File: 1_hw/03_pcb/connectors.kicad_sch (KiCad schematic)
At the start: 15 parts, among them J1 TYPE-C-31-M-12, J2 SMA, J3 SMA, J4 BNC, J5 PH-00244

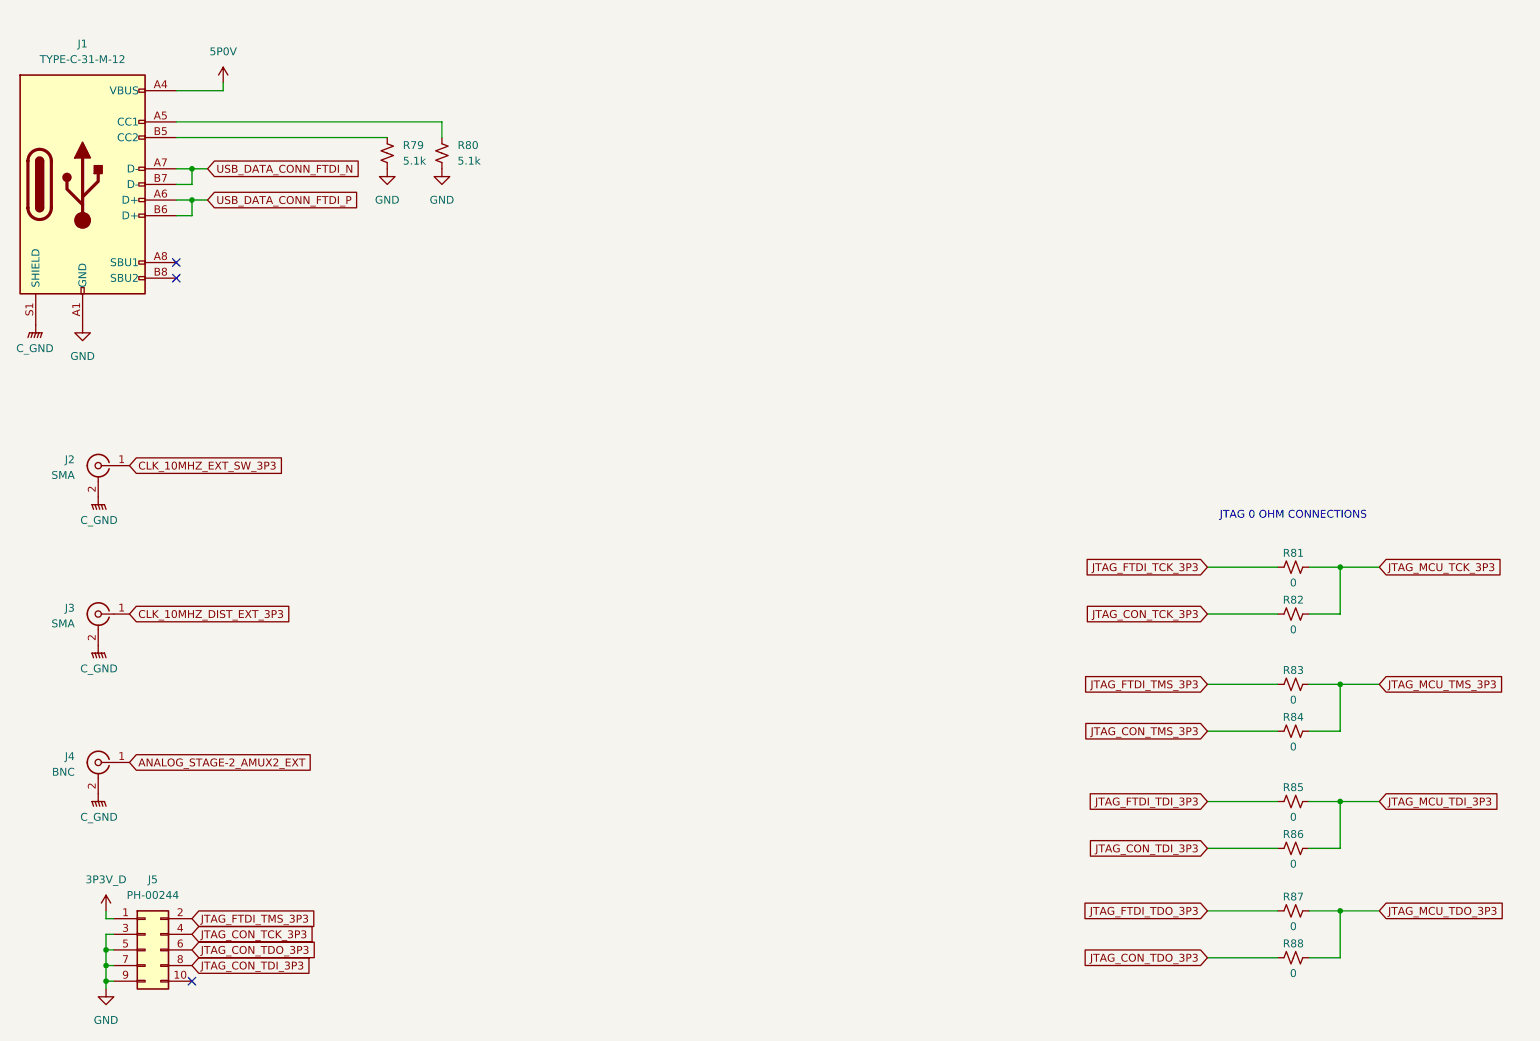
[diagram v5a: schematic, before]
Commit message: FEAT: Added MCU Flash. Finished creating & assigning footprints. Ran ERC & cleared out issues. Ready for Layout.
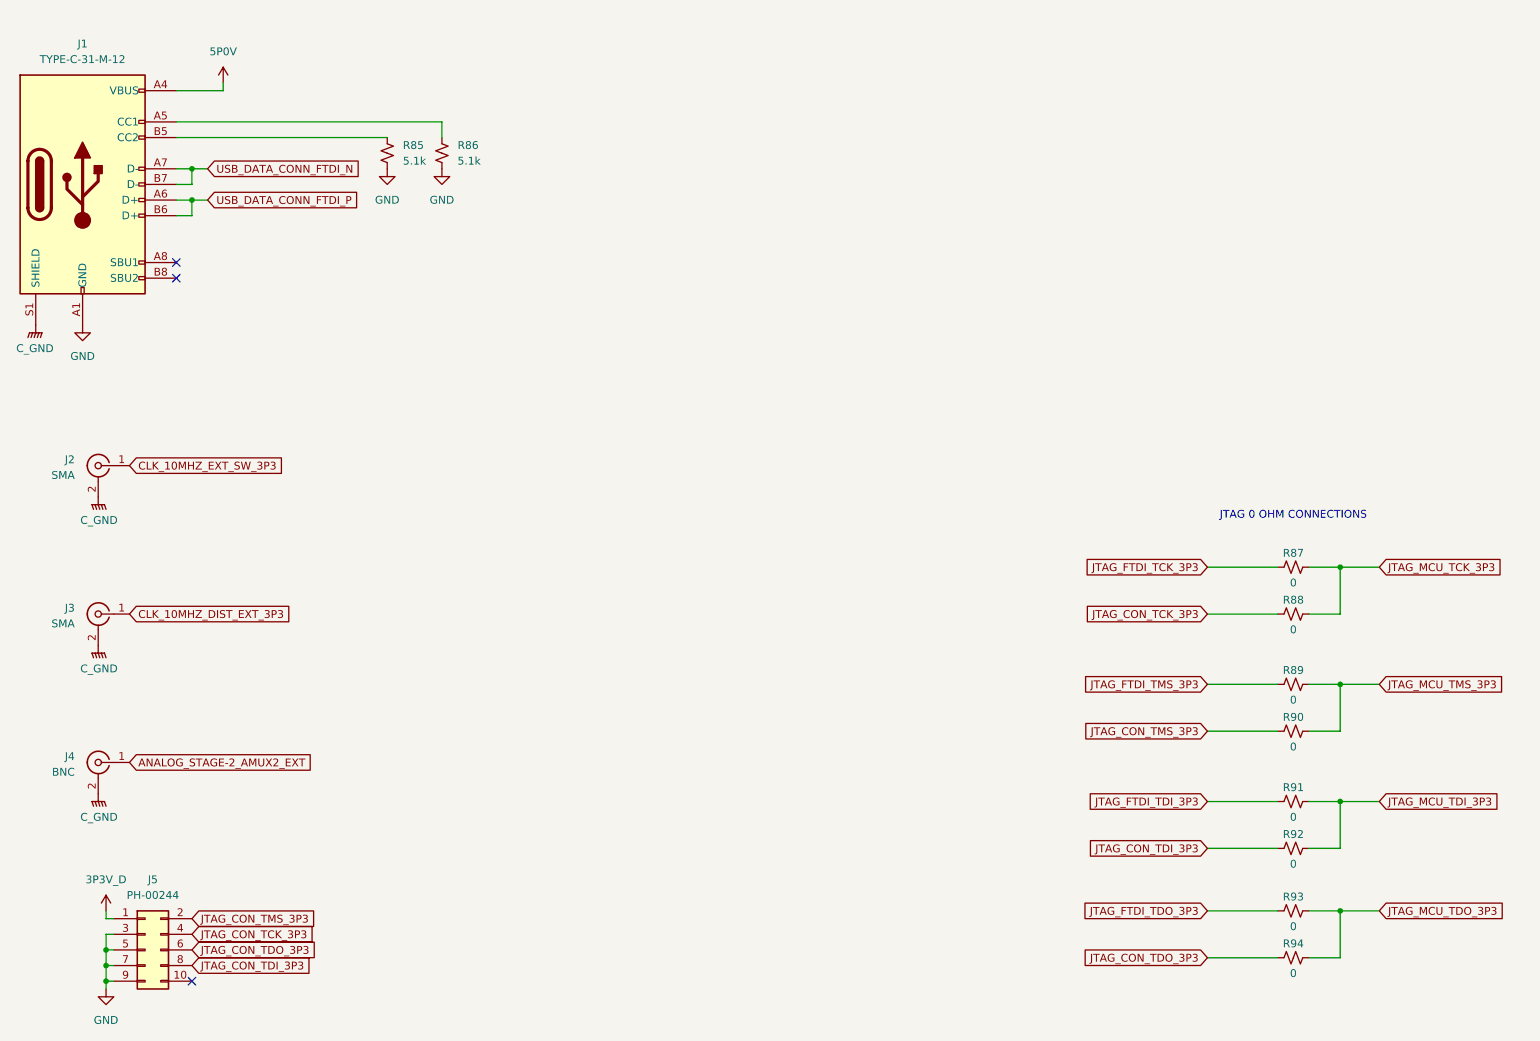
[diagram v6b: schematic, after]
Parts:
- renumbered R79 to R85, R80 to R86, R81 to R87, R82 to R88, R83 to R89, R84 to R90, R85 to R91, R86 to R92, R87 to R93, R88 to R94
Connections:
- net JTAG_CON_TMS_3P3: now also J5.2 (Pin_2)
- net JTAG_FTDI_TMS_3P3: no longer J5.2 (Pin_2)
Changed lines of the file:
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@@
 		)
 	)
-	(global_label "JTAG_FTDI_TMS_3P3"
+	(global_label "JTAG_CON_TMS_3P3"
 		(shape input)
 		(at 50.8 161.29 0)
@@
 		(on_board yes)
 		(dnp no)
-		(property "Reference" "R88"
+		(property "Reference" "R94"
 			(at 229.87 165.354 90)
 			(effects
@@
 			(project "arb"
 				(path "/866ef9be-3b01-4288-a6e0-a2357aa17e50/eb105004-087f-4ea7-8291-809b214299af"
-					(reference "R88")
+					(reference "R94")
 					(unit 1)
 				)
@@
 		(dnp no)
 		(fields_autoplaced yes)
-		(property "Reference" "#PWR0266"
+		(property "Reference" "#PWR0281"
 			(at 35.56 121.92 0)
 			(effects
@@
 			)
 		)
-		(property "Description" "CHASSIS GROUND"
+		(property "Description" "Power symbol creates a global label with name \"GNDPWR\" , global ground"
 			(at 35.56 116.84 0)
 			(effects
@@
 			(project "arb"
 				(path "/866ef9be-3b01-4288-a6e0-a2357aa17e50/eb105004-087f-4ea7-8291-809b214299af"
-					(reference "#PWR0266")
+					(reference "#PWR0281")
 					(unit 1)
 				)
@@
 			)
 		)
-		(property "Description" "BNC Connector, Through-Hole, Horizontal"
+		(property "Description" "coaxial connector (BNC, SMA, SMB, SMC, Cinch/RCA, LEMO, ...)"
 			(at 35.56 135.89 0)
 			(effects
@@
 		(dnp no)
 		(fields_autoplaced yes)
-		(property "Reference" "#PWR0268"
+		(property "Reference" "#PWR0283"
 			(at 36.83 163.83 0)
 			(effects
@@
 			(project "arb"
 				(path "/866ef9be-3b01-4288-a6e0-a2357aa17e50/eb105004-087f-4ea7-8291-809b214299af"
-					(reference "#PWR0268")
+					(reference "#PWR0283")
 					(unit 1)
 				)
@@
 		(on_board yes)
 		(dnp no)
-		(property "Reference" "R83"
+		(property "Reference" "R89"
 			(at 229.87 120.904 90)
 			(effects
@@
 			(project "arb"
 				(path "/866ef9be-3b01-4288-a6e0-a2357aa17e50/eb105004-087f-4ea7-8291-809b214299af"
-					(reference "R83")
+					(reference "R89")
 					(unit 1)
 				)
@@
 		(dnp no)
 		(fields_autoplaced yes)
-		(property "Reference" "R80"
+		(property "Reference" "R86"
 			(at 93.98 35.5599 0)
 			(effects
@@
 			(project "arb"
 				(path "/866ef9be-3b01-4288-a6e0-a2357aa17e50/eb105004-087f-4ea7-8291-809b214299af"
-					(reference "R80")
+					(reference "R86")
 					(unit 1)
 				)
@@
 			)
 		)
-		(property "Description" "SMA Connector, Through-Hole, Horizontal"
+		(property "Description" "coaxial connector (BNC, SMA, SMB, SMC, Cinch/RCA, LEMO, ...)"
 			(at 35.56 87.63 0)
 			(effects
@@
 		(dnp no)
 		(fields_autoplaced yes)
-		(property "Reference" "#PWR0271"
+		(property "Reference" "#PWR0286"
 			(at 82.55 45.72 0)
 			(effects
@@
 			(project "arb"
 				(path "/866ef9be-3b01-4288-a6e0-a2357aa17e50/eb105004-087f-4ea7-8291-809b214299af"
-					(reference "#PWR0271")
+					(reference "#PWR0286")
 					(unit 1)
 				)
@@
 		(dnp no)
 		(fields_autoplaced yes)
-		(property "Reference" "#PWR0267"
+		(property "Reference" "#PWR0282"
 			(at 35.56 146.05 0)
 			(effects
@@
 			)
 		)
-		(property "Description" "CHASSIS GROUND"
+		(property "Description" "Power symbol creates a global label with name \"GNDPWR\" , global ground"
 			(at 35.56 140.97 0)
 			(effects
@@
 			(project "arb"
 				(path "/866ef9be-3b01-4288-a6e0-a2357aa17e50/eb105004-087f-4ea7-8291-809b214299af"
-					(reference "#PWR0267")
+					(reference "#PWR0282")
 					(unit 1)
 				)
@@
 		(dnp no)
 		(fields_autoplaced yes)
-		(property "Reference" "#PWR0269"
+		(property "Reference" "#PWR0284"
 			(at 36.83 179.07 0)
 			(effects
@@
 			(project "arb"
 				(path "/866ef9be-3b01-4288-a6e0-a2357aa17e50/eb105004-087f-4ea7-8291-809b214299af"
-					(reference "#PWR0269")
+					(reference "#PWR0284")
 					(unit 1)
 				)
@@
 			)
 		)
-		(property "Description" "SMA Connector, Through-Hole, Horizontal"
+		(property "Description" "coaxial connector (BNC, SMA, SMB, SMC, Cinch/RCA, LEMO, ...)"
 			(at 35.56 111.76 0)
 			(effects
@@
 		(dnp no)
 		(fields_autoplaced yes)
-		(property "Reference" "#PWR0272"
+		(property "Reference" "#PWR0287"
 			(at 91.44 45.72 0)
 			(effects
@@
 			(project "arb"
 				(path "/866ef9be-3b01-4288-a6e0-a2357aa17e50/eb105004-087f-4ea7-8291-809b214299af"
-					(reference "#PWR0272")
+					(reference "#PWR0287")
 					(unit 1)
 				)
@@
 		(dnp no)
 		(fields_autoplaced yes)
-		(property "Reference" "#PWR0263"
+		(property "Reference" "#PWR0278"
 			(at 25.4 69.85 0)
 			(effects
@@
 			)
 		)
-		(property "Description" "CHASSIS GROUND"
+		(property "Description" "Power symbol creates a global label with name \"GNDPWR\" , global ground"
 			(at 25.4 64.77 0)
 			(effects
@@
 			(project "arb"
 				(path "/866ef9be-3b01-4288-a6e0-a2357aa17e50/eb105004-087f-4ea7-8291-809b214299af"
-					(reference "#PWR0263")
+					(reference "#PWR0278")
 					(unit 1)
 				)
@@
 		(on_board yes)
 		(dnp no)
-		(property "Reference" "R82"
+		(property "Reference" "R88"
 			(at 229.87 109.474 90)
 			(effects
@@
 			(project "arb"
 				(path "/866ef9be-3b01-4288-a6e0-a2357aa17e50/eb105004-087f-4ea7-8291-809b214299af"
-					(reference "R82")
+					(reference "R88")
 					(unit 1)
 				)
@@
 		(on_board yes)
 		(dnp no)
-		(property "Reference" "R85"
+		(property "Reference" "R91"
 			(at 229.87 139.954 90)
 			(effects
@@
 			(project "arb"
 				(path "/866ef9be-3b01-4288-a6e0-a2357aa17e50/eb105004-087f-4ea7-8291-809b214299af"
-					(reference "R85")
+					(reference "R91")
 					(unit 1)
 				)
@@
 		(dnp no)
 		(fields_autoplaced yes)
-		(property "Reference" "#PWR0264"
+		(property "Reference" "#PWR0279"
 			(at 33.02 71.12 0)
 			(effects
@@
 			(project "arb"
 				(path "/866ef9be-3b01-4288-a6e0-a2357aa17e50/eb105004-087f-4ea7-8291-809b214299af"
-					(reference "#PWR0264")
+					(reference "#PWR0279")
 					(unit 1)
 				)
@@
 		(on_board yes)
 		(dnp no)
-		(property "Reference" "R86"
+		(property "Reference" "R92"
 			(at 229.87 147.574 90)
 			(effects
@@
 			(project "arb"
 				(path "/866ef9be-3b01-4288-a6e0-a2357aa17e50/eb105004-087f-4ea7-8291-809b214299af"
-					(reference "R86")
+					(reference "R92")
 					(unit 1)
 				)
@@
 		(on_board yes)
 		(dnp no)
-		(property "Reference" "R87"
+		(property "Reference" "R93"
 			(at 229.87 157.734 90)
 			(effects
@@
 			(project "arb"
 				(path "/866ef9be-3b01-4288-a6e0-a2357aa17e50/eb105004-087f-4ea7-8291-809b214299af"
-					(reference "R87")
+					(reference "R93")
 					(unit 1)
 				)
@@
 		(on_board yes)
 		(dnp no)
-		(property "Reference" "R81"
+		(property "Reference" "R87"
 			(at 229.87 101.854 90)
 			(effects
@@
 			(project "arb"
 				(path "/866ef9be-3b01-4288-a6e0-a2357aa17e50/eb105004-087f-4ea7-8291-809b214299af"
-					(reference "R81")
+					(reference "R87")
 					(unit 1)
 				)
@@
 		(dnp no)
 		(fields_autoplaced yes)
-		(property "Reference" "#PWR0270"
+		(property "Reference" "#PWR0285"
 			(at 55.88 29.21 0)
 			(effects
@@
 			(project "arb"
 				(path "/866ef9be-3b01-4288-a6e0-a2357aa17e50/eb105004-087f-4ea7-8291-809b214299af"
-					(reference "#PWR0270")
+					(reference "#PWR0285")
 					(unit 1)
 				)
@@
 		(dnp no)
 		(fields_autoplaced yes)
-		(property "Reference" "R79"
+		(property "Reference" "R85"
 			(at 85.09 35.5599 0)
 			(effects
@@
 			(project "arb"
 				(path "/866ef9be-3b01-4288-a6e0-a2357aa17e50/eb105004-087f-4ea7-8291-809b214299af"
-					(reference "R79")
+					(reference "R85")
 					(unit 1)
 				)
@@
 		(dnp no)
 		(fields_autoplaced yes)
-		(property "Reference" "#PWR0265"
+		(property "Reference" "#PWR0280"
 			(at 35.56 97.79 0)
 			(effects
@@
 			)
 		)
-		(property "Description" "CHASSIS GROUND"
+		(property "Description" "Power symbol creates a global label with name \"GNDPWR\" , global ground"
 			(at 35.56 92.71 0)
 			(effects
@@
 			(project "arb"
 				(path "/866ef9be-3b01-4288-a6e0-a2357aa17e50/eb105004-087f-4ea7-8291-809b214299af"
-					(reference "#PWR0265")
+					(reference "#PWR0280")
 					(unit 1)
 				)
@@
 		(on_board yes)
 		(dnp no)
-		(property "Reference" "R84"
+		(property "Reference" "R90"
 			(at 229.87 128.524 90)
 			(effects
@@
 			(project "arb"
 				(path "/866ef9be-3b01-4288-a6e0-a2357aa17e50/eb105004-087f-4ea7-8291-809b214299af"
-					(reference "R84")
-					(unit 1)
-				)
+					(reference "R90")
+					(unit 1)
+				)
